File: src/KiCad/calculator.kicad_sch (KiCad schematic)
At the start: 20 parts, among them SW1 1, SW10 0, SW11 ., SW12 x10, SW13 DEL, SW14 x, SW15 +, SW16 Ans, SW17 AC, SW18 /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

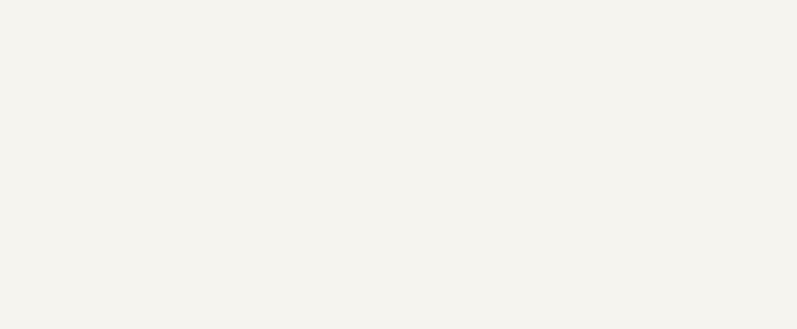
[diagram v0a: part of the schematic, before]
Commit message: Add four push switches; update README & .gitignore
Add four push-button switch symbols (SW21–SW24) to src/KiCad/calculator.kicad_sch and update used_designators in src/KiCad/calculator.kicad_pro from "SW1-20" to "SW1-24". Also add src/kicad/calculator-backups to .gitignore and update README with a live schematic link and a note about future firmware releases.
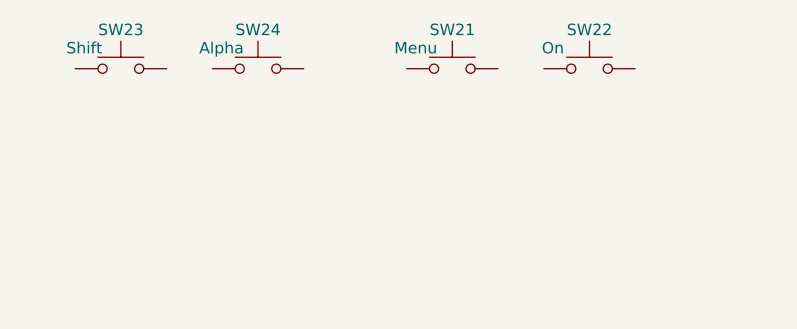
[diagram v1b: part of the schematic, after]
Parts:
- added SW21: Menu, symbol Switch:SW_Push
- added SW22: On, symbol Switch:SW_Push
- added SW23: Shift, symbol Switch:SW_Push
- added SW24: Alpha, symbol Switch:SW_Push

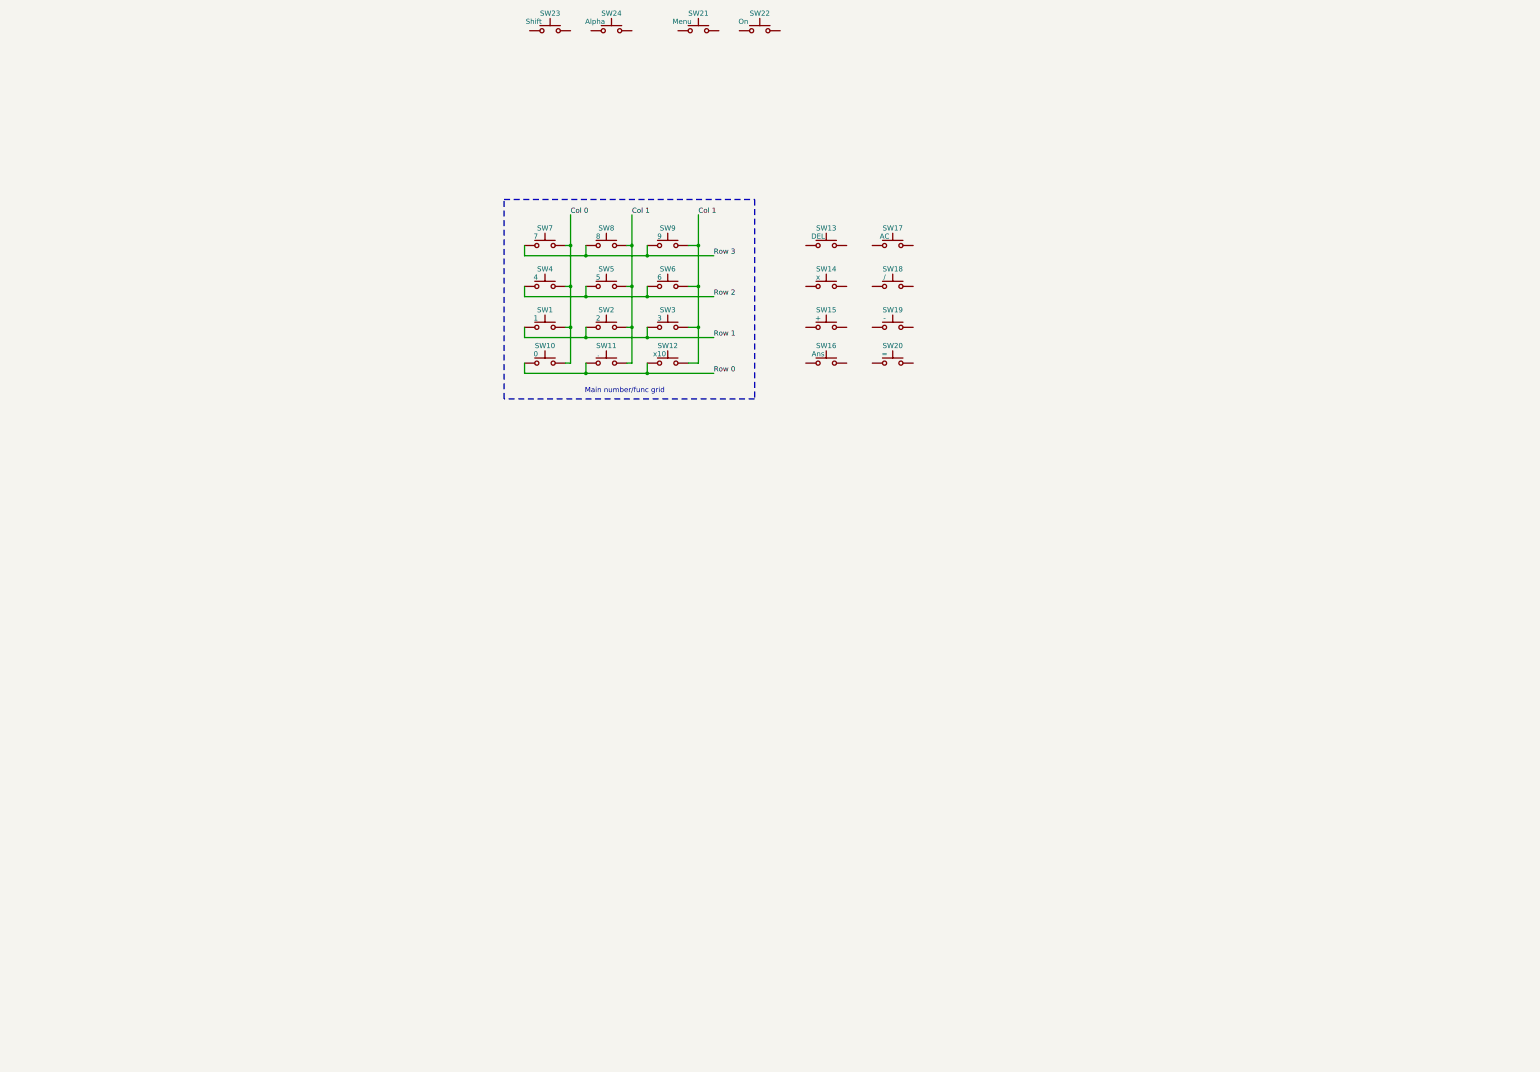
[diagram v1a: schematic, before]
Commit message: Add USB-C connector symbol and update schematic
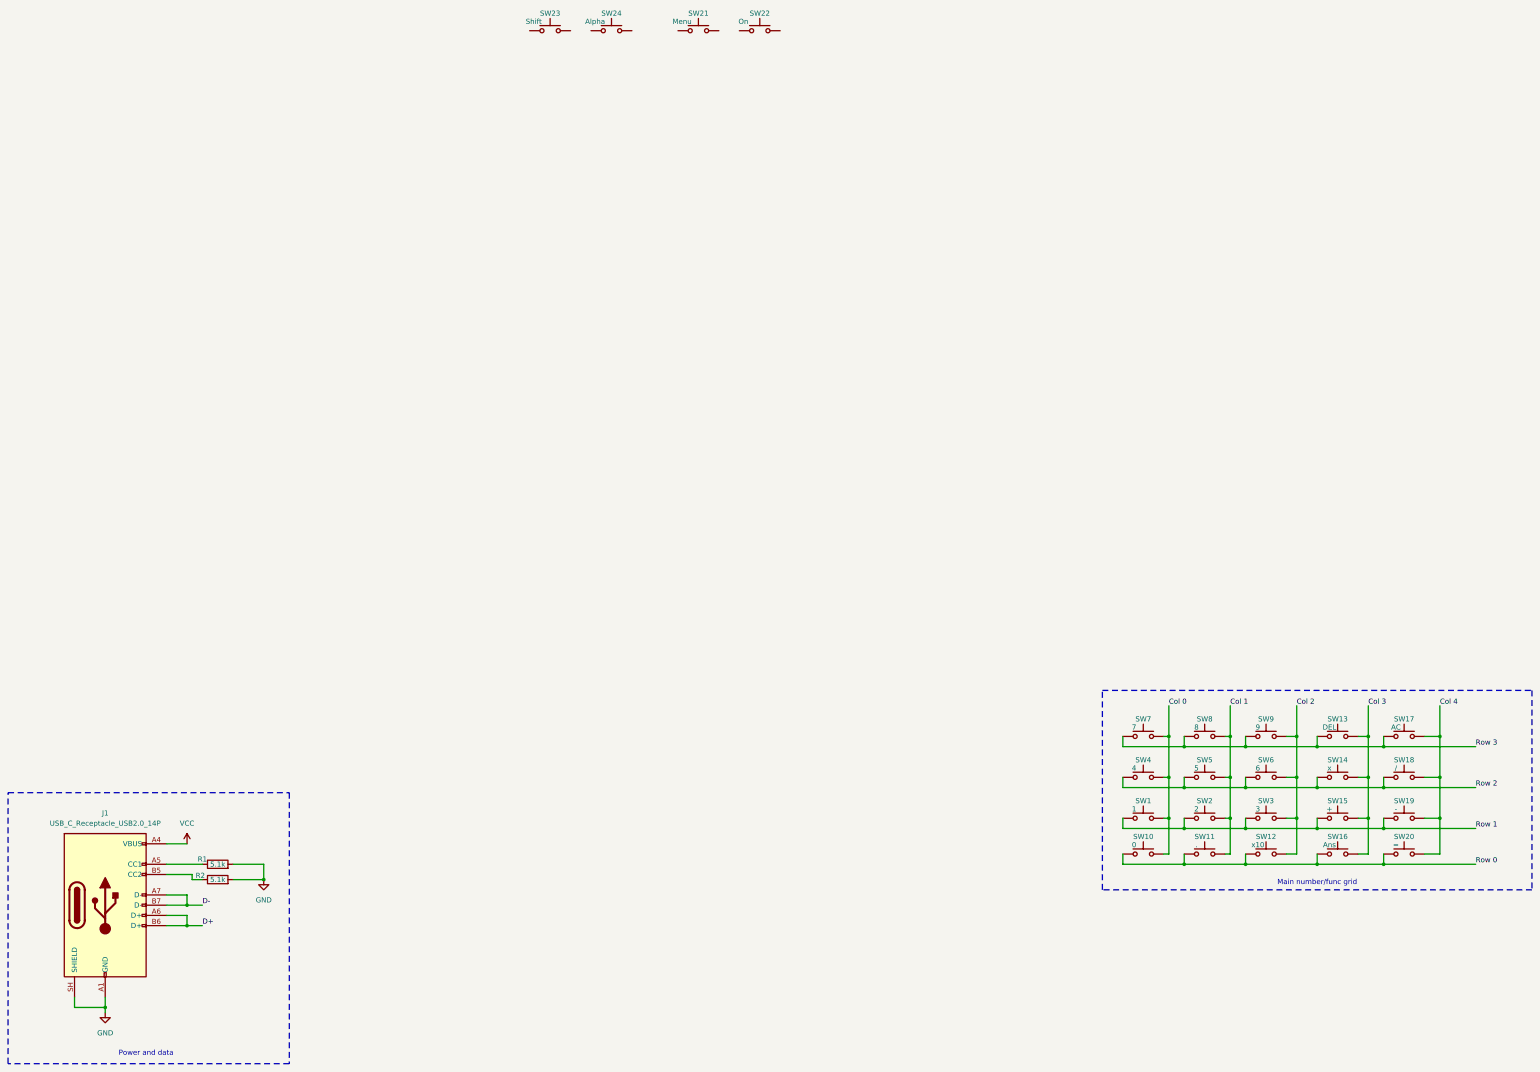
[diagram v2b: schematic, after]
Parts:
- added J1: USB_C_Receptacle_USB2.0_14P, symbol Connector:USB_C_Receptacle_USB2.0_14P
- added R1, R2: 5.1k, symbol Device:R
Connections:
- net Col 1: no longer SW12.2, SW3.2, SW6.2, SW9.2
- net Row 0: now also SW16.1, SW20.1
- net Row 1: now also SW15.1, SW19.1
- net Row 2: now also SW14.1, SW18.1
- net Row 3: now also SW13.1, SW17.1
- net Col 4: now reaches SW19.2
- net Col 4: now also SW17.2, SW18.2, SW20.2
- net Col 3: now reaches SW13.2
- net Col 3: now also SW14.2, SW15.2, SW16.2
- new net: J1.A5 (CC1), R1.1
- new net: J1.B5 (CC2), R2.1
- new net Col 2: SW12.2, SW3.2, SW6.2, SW9.2
- new net D+: J1.A6 (D+), J1.B6 (D+)
- new net D-: J1.A7 (D-), J1.B7 (D-)
- new net GND: J1.A1 (GND), J1.A12 (GND), J1.B1 (GND), J1.B12 (GND), J1.SH (SHIELD), R1.2, R2.2
- new net VCC: J1.A4 (VBUS), J1.A9 (VBUS), J1.B4 (VBUS), J1.B9 (VBUS)
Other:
- note added: "Power and data"
- moved on the sheet: SW1, SW10, SW11, SW12, SW13, SW14, SW15, SW16, SW17, SW18, SW19, SW2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

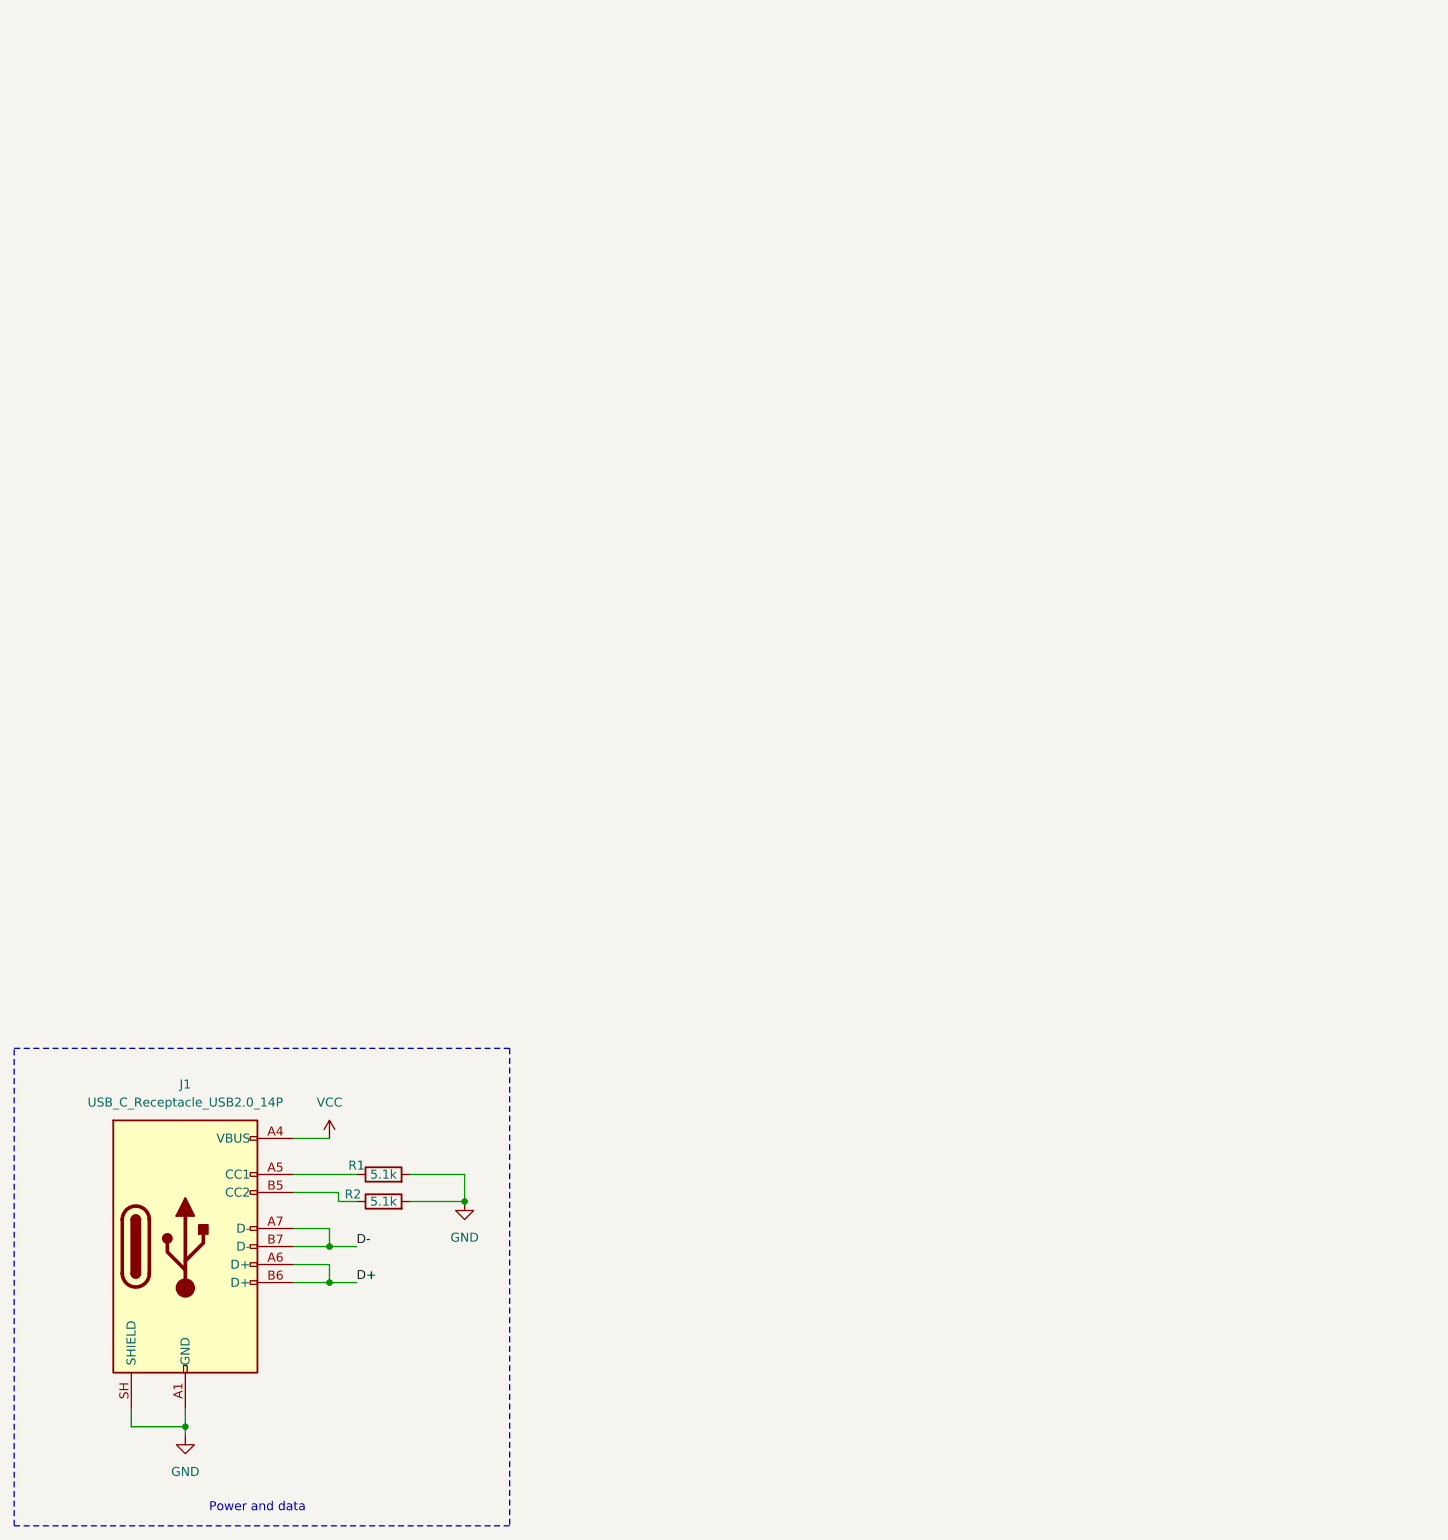
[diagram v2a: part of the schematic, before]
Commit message: battery charging and add regulator
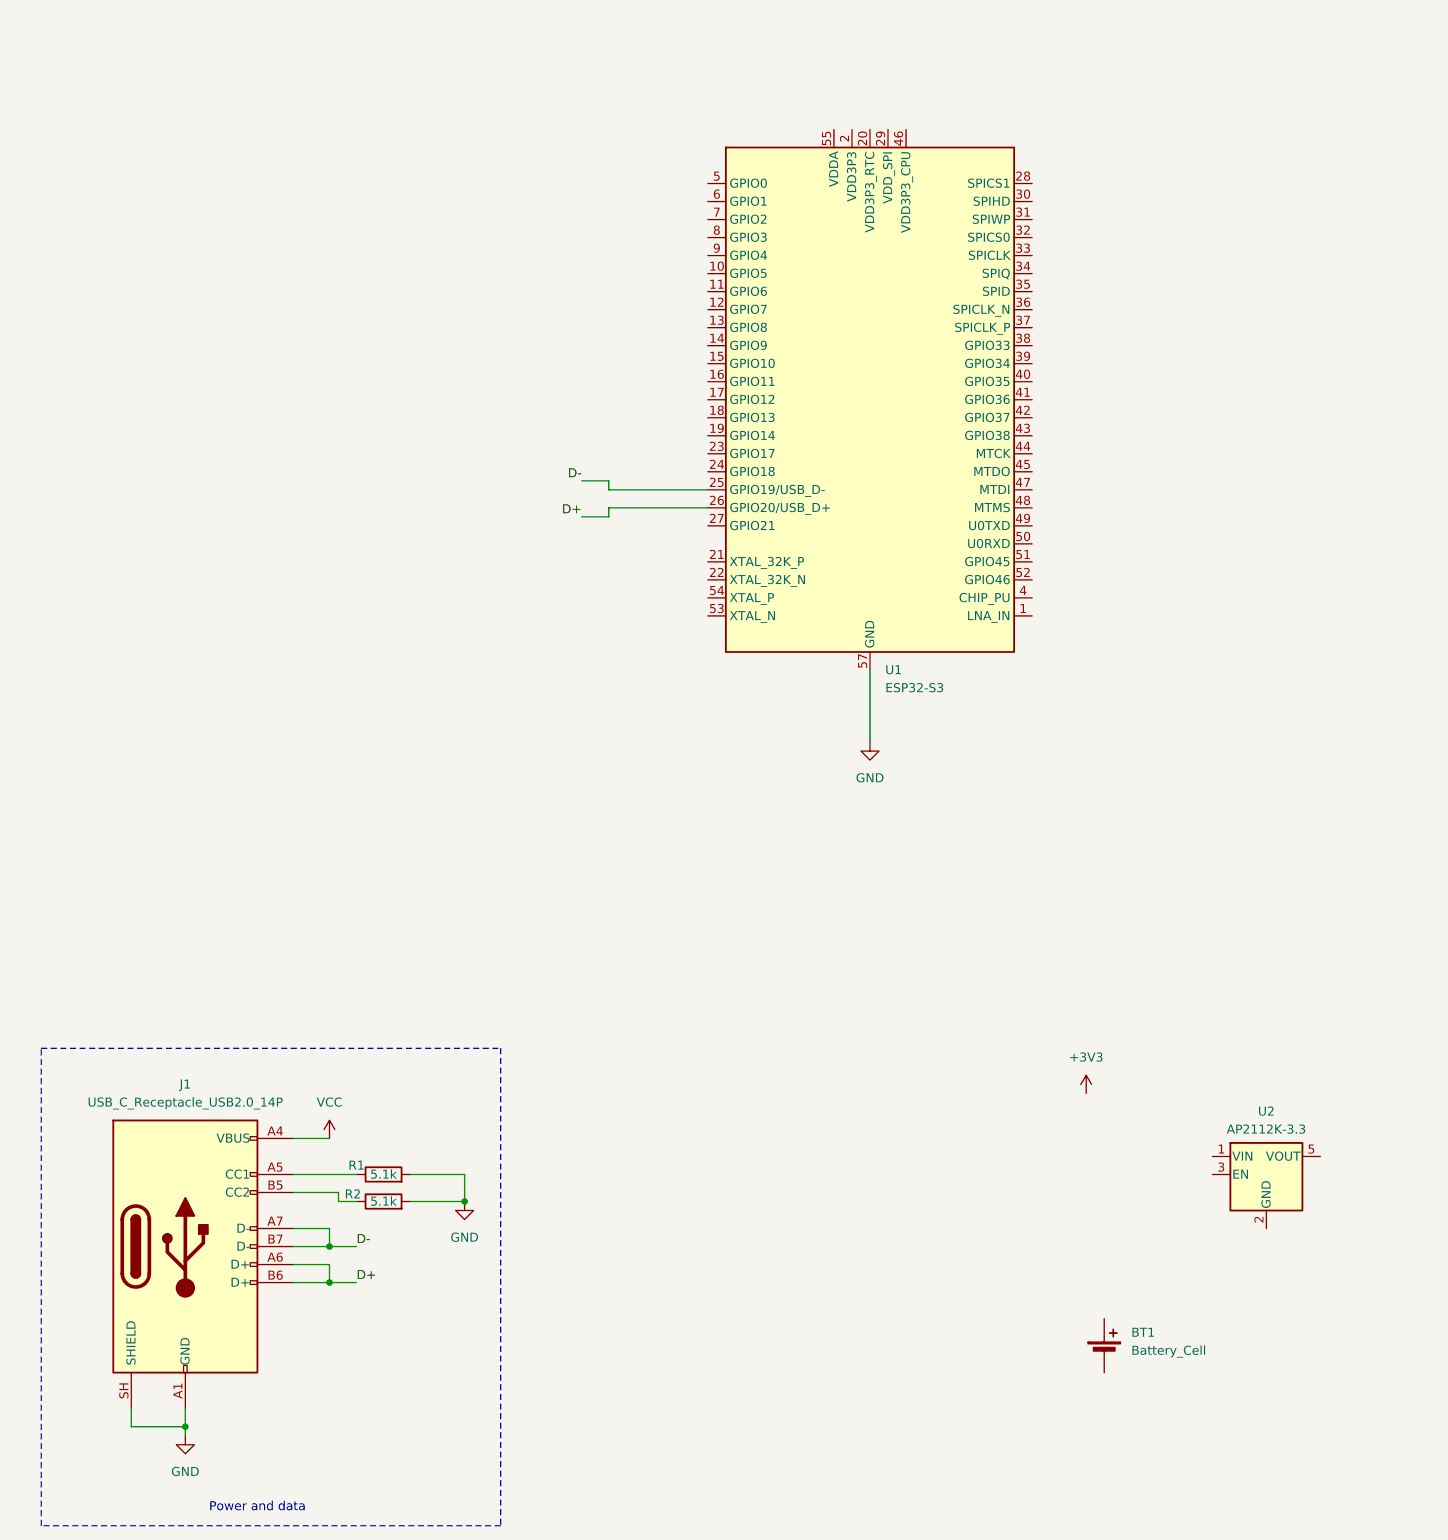
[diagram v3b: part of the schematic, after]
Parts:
- added BT1: Battery_Cell, symbol Device:Battery_Cell
- added U1: ESP32-S3, Package_DFN_QFN:QFN-56-1EP_7x7mm_P0.4mm_EP4x4mm, symbol MCU_Espressif:ESP32-S3
- added U2: AP2112K-3.3, Package_TO_SOT_SMD:SOT-23-5, symbol Regulator_Linear:AP2112K-3.3
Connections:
- net D+: now also U1.26 (GPIO20/USB_D+)
- net D-: now also U1.25 (GPIO19/USB_D-)
- net GND: now also U1.57 (GND)
- new net: U1.2 (VDD3P3), U1.3 (VDD3P3)
- new net: U1.55 (VDDA), U1.56 (VDDA)
